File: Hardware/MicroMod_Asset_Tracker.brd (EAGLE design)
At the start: 58.4 x 52.1 mm, 215 parts, among them J11 microSD, J17 NANO_SIM, J18 SARA_USB, J2 JTAG, J3 QWIIC_RIGHT_ANGLE, J4 MICROMOD-2222-C, J5 SPI, J6 SPI, J7 QWIIC_RIGHT_ANGLE, Q1 20V/0.2A/8MHz/1.2Ω/1Vth, Q10 20V/0.2A/8MHz/1.2Ω/1Vth, Q2 310mA/60V/1.6Ω, Q3 20V/0.2A/8MHz/1.2Ω/1Vth, Q4 310mA/60V/1.6Ω, Q5 20V/0.2A/8MHz/1.2Ω/1Vth, Q6 20V/4.2A/52mΩ/1.4W, Q7 20V/0.2A/8MHz/1.2Ω/1Vth, Q9 20V/0.2A/8MHz/1.2Ω/1Vth, U1 SARA-R5, U13 9DoF IMU, U14 1.8V/100mA, U2 MCP73831, U3 3.3V, U4 TXB0104, U5 AP7361C-33FGE, U6 TXB0104, U7 PCA9306, U8 74HC1G04

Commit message: Almost ready for airwire review
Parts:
- removed Q7, Q9: 20V/0.2A/8MHz/1.2Ω/1Vth, SparkFun-DiscreteSemi:SOT-416FL
- removed R40, R41, R44, R45, R46, R47: 2.2k, SparkFun-Resistors:0402-TIGHT
- removed U$75, U$76: (no value), output:#RX1#6
- removed U$79, U$80: (no value), output:#TX1#5
- added D12: GREEN, SparkFun-LED:LED-0603
- added D13: BLUE, SparkFun-LED:LED-0603
- added JP6: JUMPER-SMT_2_NC_TRACE_SILK, SparkFun-Jumpers:SMT-JUMPER_2_NC_TRACE_SILK
- added LOGO6: QWIIC_LOGO_CONNECTOR, SparkFun-Aesthetics:QWIIC_5.5MM
- added R31, R36, R37: 0, SparkFun-Resistors:0603
- added R32, R33, R34, R35: 1k, SparkFun-Resistors:0603
- added U$22: (no value), output:#GND#0
- added U$26, U$27: (no value), output:#SCL#3
- added U$3: (no value), output:#3V3#1
- added U$30, U$37: (no value), output:#SDA#2
- added U$53: (no value), output:#I�C#0
- added U$54: (no value), output:Z0
- added U9: TXB0104, SparkFun-IC-Comms:TSSOP14
- C6: device SparkFun-Capacitors:0402-TIGHT -> SparkFun-Capacitors:0603
- Q1, Q3: value 20V/0.2A/8MHz/1.2Ω/1Vth -> 310mA/60V/1.6Ω; device SparkFun-DiscreteSemi:SOT-416FL -> SparkFun-DiscreteSemi:SOT323
- R14, R21: device SparkFun-Resistors:0402-TIGHT -> SparkFun-Resistors:0603
- U$11: device output:#GND#0 -> output:#3V3#1
- U$38: device output:22223 -> output:Y2
- U$39: device output:ACCEL4 -> output:X1
- moved R30 155.9 mm to (52.7, 72.9), turned to 90 degrees
- moved R29 154.8 mm to (49.1, 72.4), turned to 90 degrees
- moved Q5 154.5 mm to (51.4, 72.4), turned to 270 degrees
- moved R26 142.6 mm to (54.9, 52.7), turned to 270 degrees
- moved R28 142.5 mm to (49.5, 47.6), turned to 90 degrees
- moved U7 142.3 mm to (54.6, 57.1), turned to 270 degrees
- moved U8 141.9 mm to (51.8, 47.6), turned to 180 degrees
- moved C21 141.0 mm to (60.6, 62.2)
- moved Q4 140.8 mm to (48.6, 50.8), turned to 90 degrees
- moved D11 139.1 mm to (53.3, 67.2), turned to 90 degrees
- moved R25 138.4 mm to (60.7, 49.5)
- moved C20 137.3 mm to (60.6, 57.1)
- moved R27 136.7 mm to (47.2, 47.6), turned to 90 degrees
- moved C17 136.1 mm to (60.6, 55.6)
- moved R24 135.8 mm to (59.7, 59.7), turned to 90 degrees
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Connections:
- new net N$29: JP6.1, R22.2
- new net N$31: R31.2, U1.4
- new net N$32: Q1.1, R32.2
- new net N$33: Q1.3, R33.1
- new net N$34: D12.C, R33.2
- new net N$35: Q3.1, R34.2
- new net N$36: Q3.3, R35.1
- new net N$37: D13.C, R35.2
- new net N$38: R36.2, U1.13
- new net N$39: R37.2, U1.12
- new net SARA_NI: R34.1, U1.16
- new net SARA_TP: R32.1, U1.19
- net 1.8V: now also U9.1, U9.8
- net 3.3V: now also D12.A, D13.A, JP6.2, U9.14; no longer R22.2, R45.2, R47.2
- net GND: now also Q1.2, Q3.2, U9.7
- net ICM-20948-LV_!CS!: now also U9.5; no longer Q9.2, R46.1
- net ICM-20948-LV_#_1.8V: no longer Q1.1, Q3.1, Q7.1, Q9.1, R40.2, R41.2, R44.2, R46.2
- net ICM-20948-LV_INT: now also U9.2; no longer Q7.2, R44.1
- net ICM-20948-LV_SCK: now also U9.4; no longer Q1.2, R40.1
- net ICM-20948-LV_SDI: now also U9.3; no longer Q3.2, R41.1
- net ICM_!CS!: now also U9.10; no longer Q9.3, R47.1
- net ICM_INT: now also U9.13; no longer Q7.3, R45.1
- net SARA_RXD: now also R36.1; no longer U1.13
- net SARA_TXD: now also R37.1; no longer U1.12
- net SPI_SCK: now also U9.11; no longer Q1.3
- net SPI_SDO: now also U9.12; no longer Q3.3
- net VCCIO: now also R31.1; no longer U1.4
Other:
- board size 58.4 x 52.1 mm -> 76.2 x 76.2 mm

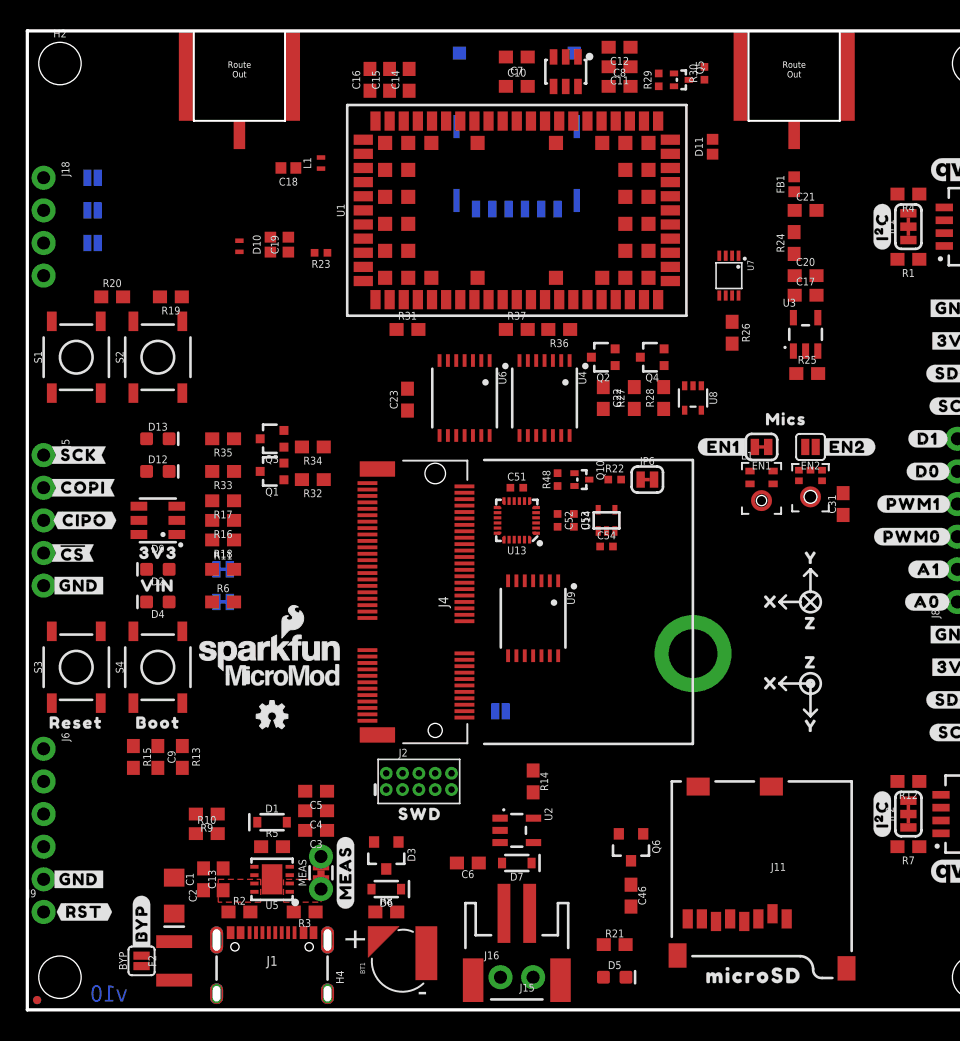
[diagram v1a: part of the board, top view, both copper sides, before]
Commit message: Ready for airwire review
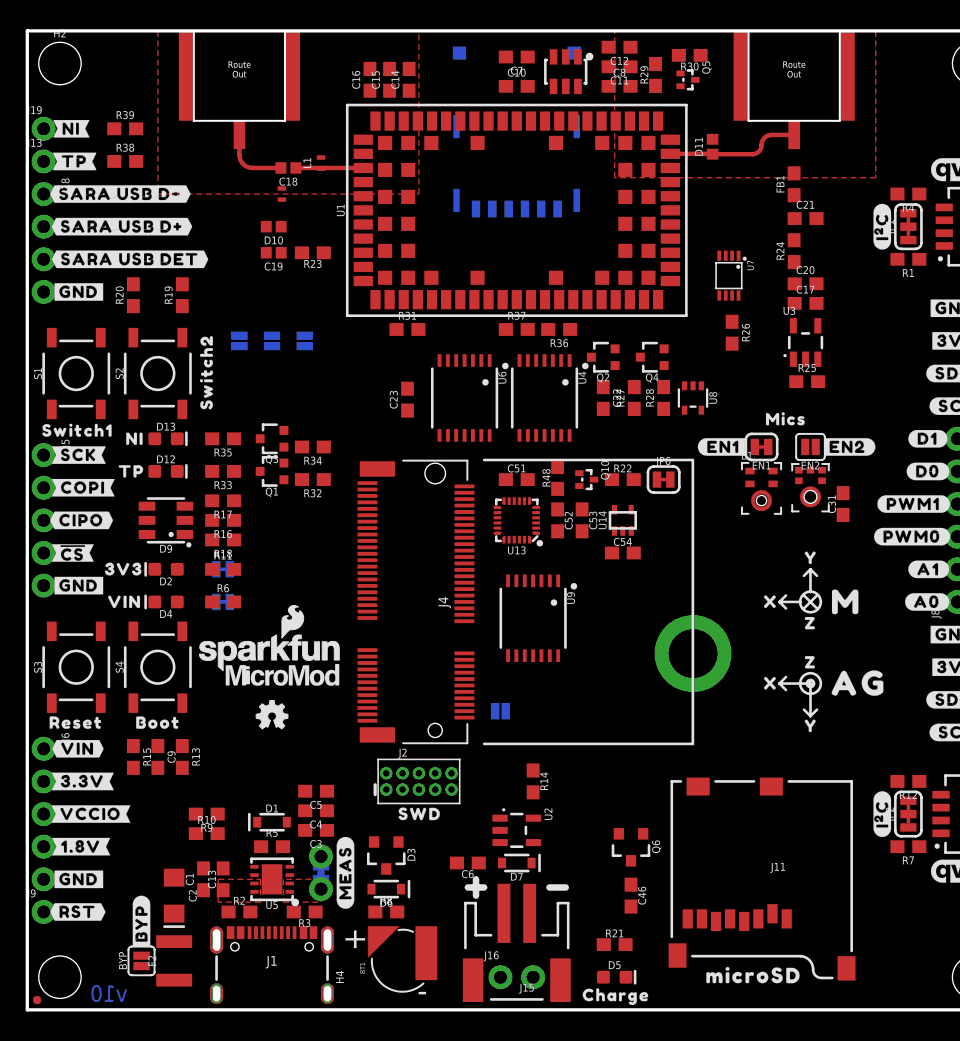
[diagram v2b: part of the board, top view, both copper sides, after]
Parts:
- added J13: TP, SparkFun-Connectors:1X01_NO_SILK
- added J19: NI, SparkFun-Connectors:1X01_NO_SILK
- added R38, R39: 100k, SparkFun-Resistors:0603
- added U$55, U$56: (no value), output:#GND#4
- added U$57, U$58: (no value), output:#TP#0
- added U$59, U$60: (no value), output:#NI#0
- added U$61, U$62, U$63, U$64: (no value), output:#SARA_USB_D##0
- added U$65, U$66: (no value), output:#SARA_USB_DET#0
- added U$67, U$75: (no value), output:#VIN#0
- added U$76, U$79: (no value), output:#3#3V#0
- added U$80, U$83: (no value), output:#VCCIO#0
- added U$84, U$85: (no value), output:#1#8V#0
- added U$86: (no value), output:#RST#1
- added U$87: (no value), output:#MEAS#2
- added U$88: (no value), output:SWITCH10
- added U$89: (no value), output:SWITCH20
- added U$90: (no value), output:NI0
- added U$91: (no value), output:TP0
- added U$92, U$93: (no value), output:#USB_D##0
- added U$94: (no value), output:#V_USB#0
- added U$95: (no value), output:AG0
- added U$96: (no value), output:M0
- added U$97: (no value), output:CHARGE0
- added U$98: (no value), output:ASSET_TRACKER0
- C51, C52, C53, C54: device SparkFun-Capacitors:0402-TIGHT -> SparkFun-Capacitors:0603
- FB1: value FERRITE_BEAD-120_OHM-0402 -> 30Ω/1.8A; device SparkFun-Coils:0402 -> SparkFun-Coils:0603
- J9: value (none) -> !RST!
- R22, R23, R29, R30, R48: device SparkFun-Resistors:0402-TIGHT -> SparkFun-Resistors:0603
- moved JP3 20.8 mm to (21.6, 52.1), turned to 90 degrees
- moved JP4 17.3 mm to (19.1, 52.1), turned to 90 degrees
- moved JP5 13.7 mm to (16.5, 52.1), turned to 90 degrees
- moved L2 5.24 mm to (19.8, 63.5)
- moved U$36 2.95 mm to (5.33, 34.3)
- moved U$46 2.84 mm to (5.59, 31.8)
- moved FRAME1 2.54 mm to (106.7, 53.3)
- moved FRAME2 2.54 mm to (106.7, 53.3)
- moved R30 1.81 mm to (51.6, 74.3), turned to 180 degrees
- moved R20 1.66 mm to (8.26, 55.6), turned to 90 degrees
- moved D10 1.42 mm to (19.2, 61.0), turned to 180 degrees
- moved C54 1.37 mm to (46.4, 35.6)
- moved C19 1.31 mm to (19.2, 58.9), turned to 180 degrees
- moved JP6 1.27 mm to (49.5, 41.3)
- moved J18 1.27 mm to (1.27, 63.5)
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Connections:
- removed net ICM-20948-LV_#_1.8V: C52.1, C53.1, Q10.1, R48.2, U13.13, U13.8, U14.5
- net 1.8V: now also C52.1, C53.1, Q10.1, R48.2, U13.13, U13.8, U14.5
- net 3.3V: now also R38.2, R39.2
- net N$33: now also J13.1, R38.1
- net N$36: now also J19.1, R39.1
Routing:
- net SARA_ANT_GNSS: track 0.00 -> 10.3 mm
- net SARA_ANT: track 0.00 -> 5.29 mm
- net N$15: track 0.00 -> 5.20 mm

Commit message: Updates to support the ESP32 PB
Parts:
- removed E2: ICS-43434, Teensy:ICS-43434
- removed EN1: (no value), SparkFun-Jumpers:SMT-JUMPER_2_NC_TRACE_SILK
- removed EN2: (no value), SparkFun-Jumpers:SMT-JUMPER_2_NO_SILK
- removed J3: QWIIC_RIGHT_ANGLE, SparkFun-Connectors:JST04_1MM_RA
- removed S4: BOOT, SparkFun-Switches:TACTILE_SWITCH_SMD_5.2MM
- added D14: WHITE, SparkFun-LED:LED-0603
- added EN: (no value), SparkFun-Jumpers:SMT-JUMPER_2_NC_TRACE_SILK
- added JP10, JP11, JP12, JP13, JP14, JP15, JP16, JP17, JP18, JP19, JP20: JUMPER-SMT_2_NC_TRACE_SILK, SparkFun-Jumpers:SMT-JUMPER_2_NC_TRACE_SILK
- added JP21, JP7, JP8, JP9: JUMPER-SMT_2_NO_SILK, SparkFun-Jumpers:SMT-JUMPER_2_NO_SILK
- added LOGO7: QWIIC_LOGO_CONNECTOR, SparkFun-Aesthetics:QWIIC_5.5MM
- added Q7: 310mA/60V/1.6Ω, SparkFun-DiscreteSemi:SOT323
- added R40, R41, R44: 100k, SparkFun-Resistors:0603
- added R42, R43: 1k, SparkFun-Resistors:0603
- added TP1, TP10, TP11, TP12, TP14, TP15, TP16, TP17, TP18, TP19, TP2, TP20, TP21, TP3, TP4, TP5, TP6, TP7, TP8, TP9: TEST-POINT3, SparkFun-Connectors:PAD.03X.03
- added U$100, U$99: (no value), output:GNSS0
- added U$101: (no value), output:ON0
- added U$102, U$105: (no value), output:#DSR#0
- added U$103: (no value), output:#SARA_INT#0
- added U$104: (no value), output:#RI#0
- added U$106: (no value), output:#SD_#CS##0
- added U$107: (no value), output:#IMU_PWR#0
- added U$108: (no value), output:#LTE_PWR#0
- added U$109: (no value), output:#SD_PWR#0
- added U$110: (no value), output:#ANT_PWR#0
- added U$111: (no value), output:#SARA_SCL#0
- added U$112: (no value), output:#SARA_SDA#0
- added U$113: (no value), output:SARA_ON0
- added U$114: (no value), output:#CIPO#0
- added U$115: (no value), output:22220
- added U$116: (no value), output:#PDM_CLK#0
- added U$117: (no value), output:#PDM_DAT#0
- added U$118, U$119: (no value), output:#SARA_ON#0
- added U$120: (no value), output:#G10#0
- added U$121: (no value), output:#G9#0
- added U$122: (no value), output:#G0#0
- added U$123: (no value), output:#G1#0
- added U$124: (no value), output:#G2#0
- added U$125: (no value), output:#G3#0
- added U$126: (no value), output:#G4#0
- added U$127: (no value), output:#G7#0
- added U$128: (no value), output:#G6#0
- added U$129: (no value), output:#G5#0
- added U$130: (no value), output:NANO_SIM0
- D9: value RGB -> 3.3V; device SparkFun-LED:PLCC-6-LED -> SparkFun-DiscreteSemi:SOD-323
- R16, R17, R18: value 1k -> 100k
- R25: value 10k -> 100k
- R33: value 1k -> 470
- S1: value SWITCH1 -> RESET
- S2: value SWITCH2 -> BOOT
- S3: value RESET -> SARA_PWR
- U$1: device output:#EN1#3 -> output:#EN#0
- U$2: device output:#EN2#4 -> output:MIC0
- U$23: device output:#I�C#0 -> output:#SARA_I�C#0
- U$35, U$68: device output:##CS##3 -> output:#D0#1
- U$5: device output:MICS0 -> output:#SARA_I�C#0
- U$88: device output:SWITCH10 -> output:LTE0
- U$89: device output:SWITCH20 -> output:LTE0
- moved D9 50.5 mm to (60.7, 45.7)
- moved LOGO6 44.0 mm to (68.6, 21.7), turned to 90 degrees
- moved R17 40.0 mm to (47.0, 15.2), turned to 0 degrees
- moved R19 35.7 mm to (46.1, 44.7), turned to 180 degrees
- moved J17 32.7 mm to (69.2, 58.4), flipped to the top, turned to 90 degrees
- moved R16 31.2 mm to (46.4, 35.6)
- moved U$88 30.1 mm to (9.02, 74.8)
- moved U$34 26.7 mm to (37.2, 63.6)
- moved LOGO4 26.7 mm to (38.1, 65.5)
- moved U$89 25.7 mm to (8.89, 74.8), flipped to the bottom, turned to 0 degrees
- moved U$98 25.4 mm to (38.1, 59.7)
- moved S1 22.9 mm to (3.81, 26.7)
- moved S2 22.9 mm to (10.2, 26.7)
- moved R20 22.4 mm to (28.6, 46.2), turned to 0 degrees
- moved R4 20.5 mm to (66.0, 43.2)
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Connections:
- removed net BLUE: J4.44, R18.1
- removed net GREEN: J4.42, R17.1, R20.1, S1.3, S1.4
- removed net I2C_!INT!: J4.16, Q5.3, R30.1
- removed net I2C_SCL1: J14.4, J3.4, J4.53, R4.1, U7.P6
- removed net I2C_SDA1: J14.3, J3.3, J4.51, R1.1, U7.P5
- removed net I2S_SD: E2.6, J4.54
- removed net RED: J4.40, R16.1
- removed net SARA_DCD: U1.8, U6.3
- removed net SARA_DSR: U1.6, U6.5
- removed net SARA_DTR: U1.9, U6.2
- removed net SARA_EXT_INT: Q5.2, R29.1, U1.33
- removed net SARA_RI: U1.7, U6.4
- removed net SPI_!CS!: J11.CS/DAT3, J4.55
- removed net SWITCH2: J4.46, R19.1, S2.3, S2.4
- new net N$40: J4.42, JP11.1
- new net N$41: J4.44, JP12.1
- new net N$42: J4.46, JP13.1
- new net N$43: J4.48, JP14.1
- new net N$44: J4.73, JP15.1
- new net N$45: J4.71, JP16.1
- new net N$46: J4.69, JP17.1
- new net N$47: Q7.1, R42.2
- new net N$48: J4.63, JP19.1
- new net N$49: D14.C, R43.2
- new net N$50: J4.65, JP21.1
- new net N$51: J4.52, JP20.1
- new net N$52: J4.50, JP18.1
- new net SARA_DCD/RXD2O: TP15.P$1, U1.8, U6.3
- new net SARA_DSR/RTS2I: TP17.P$1, U1.6, U6.5
- new net SARA_DTR/TXD2I: TP14.P$1, U1.9, U6.2
- new net SARA_INT: JP15.2, Q5.3, R30.1, TP12.P$1
- new net SARA_INT_1.8V: Q5.2, R29.1, TP11.P$1, U1.33
- new net SARA_ON: JP19.2, JP21.2, Q7.3, R43.1, R44.1
- new net SARA_RI/CTS2O: TP16.P$1, U1.7, U6.4
- new net SARA_SCL_1.8V: TP10.P$1, U1.27, U7.P3
- new net SARA_SDA_1.8V: TP9.P$1, U1.26, U7.P4
- new net SD_!CS!: J11.CS/DAT3, JP10.2, R41.1
- net !BOOT!: now also S2.3, S2.4; no longer S4.3, S4.4
- net !RESET!: now also S1.3, S1.4; no longer S3.3, S3.4
- net 3.3V: now also D14.A, EN.2, R16.2, R41.2, R44.2; no longer D9.AB, D9.AG, D9.AR, EN1.2, EN2.2, J3.2, R19.2, R20.2
- net ANT_GNSS_PWR_EN: now also D9.C, JP16.2; no longer J4.73
- net CTS1: now also TP7.P$1
- net DCD: now also J4.20, TP19.P$1; no longer J4.68
- net DSR: now also JP17.2, R20.2, TP21.P$1; no longer J4.64
- net DTR: now also J4.22, R40.1, TP18.P$1; no longer J4.70
- net GND: now also D9.A, JP9.1, Q7.2, R17.1, R18.2, R19.1, R40.2, S3.3, S3.4; no longer E2.2, E2.3, E2.7, E2.8, E2.9, J3.1, R25.1, S3.1, S3.2, S4.1, S4.2
- net I2S_SCK/PDM_CLK: now also JP18.2; no longer E2.4, J4.50
- net I2S_WS/PDM_DAT: now also JP20.2; no longer E2.1, J4.52
- net ICM_!CS!: now also J4.55; no longer J4.71
- net ICM_INT: now also J4.16; no longer J4.69
- net ICM_PWR: now also JP13.2, R16.1; no longer J4.62
- net LTE_PWR_ON: now also JP12.2, R18.1; no longer J4.48
- net MICROSD_PWR: now also JP11.2, R17.2; no longer J4.60
- net N$17: now also J4.51, JP8.2; no longer D9.CG, R17.2
- net N$18: now also JP9.2, R20.1; no longer D9.CB, R18.2
- net N$19: now also J4.40, JP10.1; no longer D9.CR, R16.2
- net N$4: now also EN.1; no longer EN1.1
- net N$5: now also J4.53, JP7.2; no longer E2.5, EN2.1
- net RI: now also JP14.2, TP20.P$1; no longer J4.66
- net RTS1: now also R19.2, TP8.P$1
- net RX1: now also TP5.P$1
- net SARA_CTS: now also TP3.P$1
- net SARA_PWR_ON: now also S3.1, S3.2
- net SARA_RTS: now also TP4.P$1
- net SARA_RXD: now also TP1.P$1
- net SARA_SCL: now also J14.4, JP7.1, R4.1, U7.P6; no longer U1.27, U7.P3
- net SARA_SDA: now also J14.3, JP8.1, R1.1, U7.P5; no longer U1.26, U7.P4
- net SARA_TXD: now also TP2.P$1
- net TX1: now also TP6.P$1
- net VCCIO: now also R42.1
- net VIN: now also R25.1

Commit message: Work in progress - 14 airwires left!
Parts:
- added U$131: (no value), output:SIM0
- U$130: device output:NANO_SIM0 -> output:NANO0
- moved R41 10.3 mm to (36.7, 17.8), turned to 270 degrees
- moved C12 10.1 mm to (36.2, 72.8), turned to 270 degrees
- moved U$19 9.38 mm to (20.8, 16.4), turned to 0 degrees
- moved C11 8.41 mm to (37.7, 72.8), turned to 270 degrees
- moved C10 6.54 mm to (44.6, 72.8), turned to 270 degrees
- moved C3 4.76 mm to (23.2, 9.27), turned to 0 degrees
- moved C4 4.76 mm to (23.2, 10.8), turned to 0 degrees
- moved C5 4.76 mm to (23.2, 12.3), turned to 0 degrees
- moved MEAS 3.76 mm to (23.6, 14.4), turned to 180 degrees
- moved U$87 3.36 mm to (26.4, 16.4), turned to 0 degrees
- moved U$130 3.07 mm to (71.1, 67.3)
- moved R5 2.07 mm to (17.7, 14.2), turned to 270 degrees
- moved C7 1.81 mm to (39.2, 72.8), turned to 90 degrees
- moved TP11 1.27 mm to (50.8, 71.1)
- moved TP1 1.27 mm to (41.9, 49.5)
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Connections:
- removed net N$23: C3.1, C4.1, C5.1, MEAS.1, MEAS.3, U5.1
- new net VREG_3.3V: C3.1, C4.1, C5.1, MEAS.1, MEAS.3, U5.1
- net SIM_CLK: now also D8.1; no longer D8.6
- net SIM_IO: now also D8.6; no longer D8.4
- net SIM_RST: now also D8.4; no longer D8.3
- net VSIM: now also D8.3; no longer D8.1
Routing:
- net VIN: track 0.00 -> 173.1 mm, vias 0 -> 10
- net VCCIO: track 0.00 -> 144.9 mm, vias 0 -> 12
- net !RESET!: track 0.00 -> 113.9 mm, vias 0 -> 2
- net 1.8V: track 0.00 -> 97.1 mm, vias 0 -> 7
- net D0: track 0.00 -> 96.3 mm, vias 0 -> 4
- net SPI_SCK: track 0.00 -> 87.4 mm, vias 0 -> 4
- net SPI_SDO: track 0.00 -> 86.2 mm, vias 0 -> 4
- net V_USB: track 0.00 -> 79.1 mm, vias 0 -> 4
- net USB_D-: track 0.00 -> 73.6 mm, vias 0 -> 5
- net SPI_SDI: track 0.00 -> 71.9 mm, vias 0 -> 2
- net SARA_USB_D+: track 0.00 -> 71.5 mm, vias 0 -> 3
- net USB_D+: track 0.00 -> 70.3 mm, vias 0 -> 3
- net SARA_USB_D-: track 0.00 -> 69.6 mm, vias 0 -> 3
- net 3.3V: track 0.00 -> 65.3 mm, vias 0 -> 22
- net SARA_VUSB_DET: track 0.00 -> 59.7 mm, vias 0 -> 3
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- added copper zone on layer 15, net 3.3V
- added copper zone on layer 2, net GND

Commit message: Ready for review
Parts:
- added TP13, TP22, TP23, TP24: TEST-POINT3, SparkFun-Connectors:PAD.03X.03
- J1: device SparkFun-Connectors:USB-C-16P-2LAYER-PADS -> SparkFun-Connectors:USB-C-16P_4LAYER-PADS
- J6: value SPI -> DIAG
- U$118, U$119: device output:#SARA_ON#0 -> output:#SARA_#ON##0
- moved VE 2.42 mm to (36.7, 20.8)
- moved U$18 2.41 mm to (35.9, 20.8)
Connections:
- net N$19 renamed G0
- net N$40 renamed G1
- net N$41 renamed G2
- net N$42 renamed G3
- net N$43 renamed G4
- net N$44 renamed G5
- net N$45 renamed G6
- net N$46 renamed G7
- net N$48 renamed G10
- net N$50 renamed G9
- removed net SARA_ON: JP19.2, JP21.2, Q7.3, R43.1, R44.1
- new net SARA_!ON!: JP19.2, JP21.2, Q7.3, R43.1, R44.1, TP13.P$1
- net N$14: now also TP24.P$1
- net N$25: now also TP22.P$1
- net SD_PWR: now also TP23.P$1
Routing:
- net RTS1: track 2.31 -> 55.5 mm, vias 1 -> 3
- net CTS1: track 2.04 -> 51.6 mm, vias 1 -> 3
- net TX1: track 2.13 -> 47.6 mm, vias 1 -> 2
- net RX1: track 1.93 -> 43.4 mm, vias 1 -> 2
- net SARA_!ON!: track 0.00 -> 33.6 mm, vias 0 -> 1
- net SARA_ON: track 31.4 -> 0.00 mm, vias 1 -> 0
- net LTE_PWR_ON: track 36.5 -> 63.8 mm, vias 1 -> 2
- net ICM_PWR: track 7.26 -> 31.6 mm, vias 0 -> 3
- net DCD: track 1.93 -> 24.2 mm, vias 1 -> 2
- net PWM1: track 42.4 -> 62.2 mm, vias 0 -> 2
- net SPI_SDI: track 71.9 -> 91.4 mm, vias 2 -> 4
- net DTR: track 11.1 -> 29.5 mm, vias 1 -> 2
- net N$14: track 3.73 -> 8.35 mm, vias 0 -> 1
- net SIM_CLK: track 47.5 -> 50.8 mm
- net SD_PWR: track 21.3 -> 24.6 mm, vias 0 -> 1
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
